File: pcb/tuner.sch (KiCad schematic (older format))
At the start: 39 parts, among them P1 PDI, SW1 SPST, SW2 <, SW3 >, SW4 Mode, U1 TPS62240, U2 NKR131SB, U3 ATXMEGA8E5, Y1 8 MHz

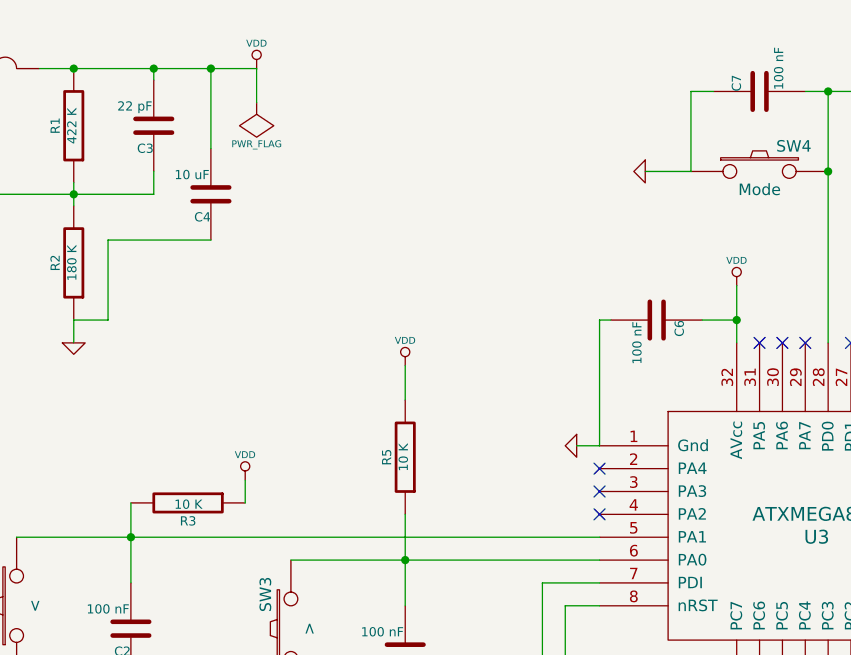
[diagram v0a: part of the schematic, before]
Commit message: - Added manufacturer, part number, and description fields to BOM - Changed MCU info to an equivalent that is available
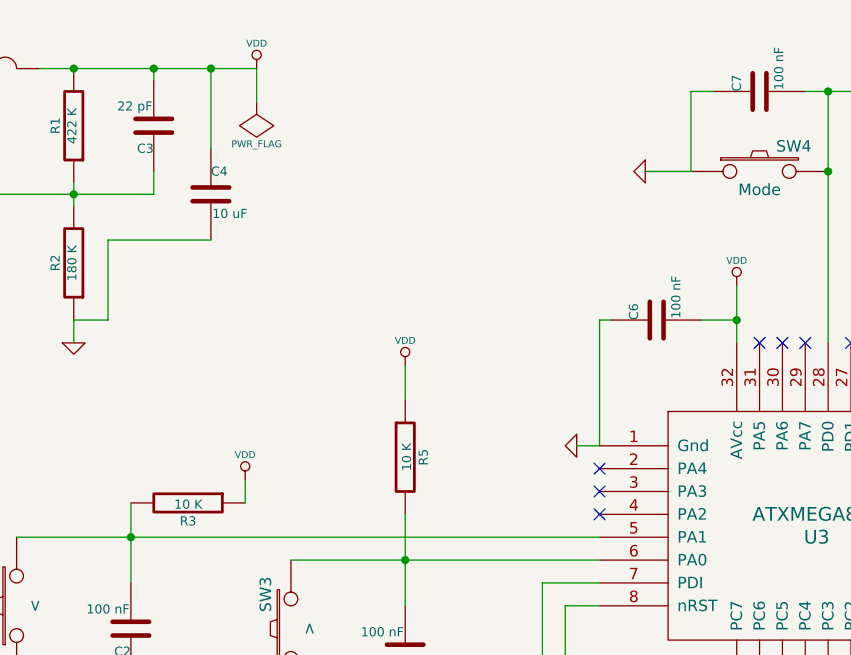
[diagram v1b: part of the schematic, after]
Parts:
- BT1: Desc (none) -> HOLDER BATT 2-AAA CELLS PC MOUNT; Manufacturer (none) -> MPD; P/N (none) -> BH2AAAPC
- C1, C4: Desc (none) -> CAP CER 10UF 6.3V 10% X5R 0805; Manufacturer (none) -> Yageo; P/N (none) -> CC0805KKX5R5BB106
- C10: Desc (none) -> CAP CER 27PF 50V 5% NP0 0805; Manufacturer (none) -> Kemet; P/N (none) -> C0805C270J5GACTU
- C2, C5, C6, C7, C8: Desc (none) -> CAP CER 0.1UF 50V 10% X7R 0805; Manufacturer (none) -> Kemet; P/N (none) -> C0805C104K5RACTU; URL http://www.digikey.ca/product-detail/en/CC0805KKX5R5BB106/3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 -> http://www.digikey.ca/product-detail/en/C0805C104K5RACTU/39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
- C3: Desc (none) -> CAP CER 22PF 50V 5% NP0 0805; Manufacturer (none) -> Kemet; P/N (none) -> C0805C220J5GACTU
- C9: Desc (none) -> CAP CER 25PF 50V 5% NP0 0805; Manufacturer (none) -> Samsung Electro-Mechanics America Inc; P/N (none) -> CL21C250JBANNNC
- D1, D2: Desc (none) -> LED 660NM SUPER RED CLR 0805 T/R; Manufacturer (none) -> Lumex Opto/Components Inc; P/N (none) -> SML-LX0805SRC-TR
- L1: Desc (none) -> INDUCTOR 2.2UH 20% 1008; Manufacturer (none) -> Murata Electronics North America; P/N (none) -> LQM2HPN2R2MJ0L
- R1: Desc (none) -> RES 422K OHM 1/8W 1% 0805 SMD; Manufacturer (none) -> Yageo; P/N (none) -> RC0805FR-07422KL
- R10, R11, R13, R14, R6, R7, R8, R9: Desc (none) -> RES 27 OHM 1/8W 1% 0805 SMD; Manufacturer (none) -> Panasonic Electronic Components; P/N (none) -> ERJ-6ENF27R0V
- R12, R3, R4, R5: Desc (none) -> RES 10.0K OHM 1/8W 1% 0805 SMD; Manufacturer (none) -> Yageo; P/N (none) -> RC0805FR-0710KL
- R15, R16: Desc (none) -> RES 18.0 OHM 1/8W 1% 0805 SMD; Manufacturer (none) -> Yageo; P/N (none) -> RC0805FR-0718RL
- R2: Desc (none) -> RES 180K OHM 1/8W 1% 0805 SMD; Manufacturer (none) -> Yageo; P/N (none) -> RC0805FR-07180KL
- SW1: Desc (none) -> SWITCH DIP SLIDE 1POS T/H 1MM 6V; Manufacturer (none) -> Copal Electronics Inc; P/N (none) -> CVS-01C
- SW2, SW3, SW4: Desc (none) -> SWITCH TACTILE SPST-NO 0.05A 12V; Manufacturer (none) -> Apem Inc.; P/N (none) -> MJTP1243
- U1: Desc (none) -> IC REG BUCK SYNC ADJ TSOT23-5; Manufacturer (none) -> Texas Instruments; P/N (none) -> TPS62240DDCT
- U2: Desc (none) -> LED 7SEG DISP .30\" RED CC BLACK; Manufacturer (none) -> Stanley Electric Co; P/N (none) -> NKR131SB
- U3: Desc (none) -> IC MCU 8BIT 8KB FLASH 32TQFP; Manufacturer (none) -> Atmel; P/N (none) -> ATXMEGA8E5-AU; URL http://www.digikey.ca/product-detail/en/ATXMEGA8E5-AUR/ATXM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 -> http://www.digikey.ca/product-detail/en/ATXMEGA8E5-AU/ATXME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
- Y1: Desc (none) -> CRYSTAL 8MHZ 18PF SMD; Manufacturer (none) -> TXC CORPORATION; P/N (none) -> 9C-8.000MEEJ-T
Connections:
- net GND: now also C4.2, C6.1; no longer C4.1, C6.2
- net VDD: now also C4.1, C6.2, R5.1; no longer C4.2, C6.1, R5.2
- net at C5.2, SW3.2, U3.6 (PA0): now also R5.2; no longer R5.1

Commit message: - Converted hardware design files to KiCAD 4.x format - Created footprints for new parts in r3 hardware design - Revised schematic and footprint associations for r3 hardware design
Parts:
- removed P1: PDI, symbol PDI
- removed R16: 18 Ohms, ~, symbol R
- removed SW1: SPST, ~, symbol SPST
- removed Y1: 8 MHz, ~, symbol CRYSTAL
- added P1: PDI, tuner:PDI_2x5, symbol SWDI
- added R16: 2.2 Ohms, Resistors_SMD:R_0603_HandSoldering, symbol R-RESCUE-tuner
- added SW1: Switch_SPDT_x2, tuner:SPDT, symbol Switch_SPDT_x2
- added Y1: 8 MHz, tuner:XTAL-SMD-4, symbol XTAL-4
- BT1: footprint (none) -> tuner:BATTERY
- C1, C4: footprint ~ -> Capacitors_SMD:C_0805_HandSoldering; symbol C -> C-RESCUE-tuner
- C10: value 27 pF -> 6.9 pF; footprint ~ -> Capacitors_SMD:C_0402; symbol C -> C-RESCUE-tuner
- C2, C3, C5, C6, C7, C8: footprint ~ -> Capacitors_SMD:C_0603_HandSoldering; symbol C -> C-RESCUE-tuner
- C9: value 25 pF -> 8.6 pF; footprint ~ -> Capacitors_SMD:C_0402; symbol C -> C-RESCUE-tuner
- D1, D2: footprint ~ -> LEDs:LED-5MM; symbol LED -> LED-RESCUE-tuner
- L1: footprint ~ -> tuner:SM1008
- R1, R10, R11, R12, R13, R14, R2, R3, R4, R5, R6, R7, R8, R9: footprint ~ -> Resistors_SMD:R_0603_HandSoldering; symbol R -> R-RESCUE-tuner
- R15: value 18 Ohms -> 2.2 Ohms; footprint ~ -> Resistors_SMD:R_0603_HandSoldering; symbol R -> R-RESCUE-tuner; Desc RES 18.0 OHM 1/8W 1% 0805 SMD -> RES SMD 2.2 OHM 1% 1/10W 0603; P/N RC0805FR-0718RL -> RC0603FR-072R2L; URL http://www.digikey.ca/product-detail/en/RC0805FR-0718RL/311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 -> https://www.digikey.ca/product-detail/en/yageo/RC0603FR-072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
- SW2, SW3, SW4: footprint ~ -> tuner:SWITCH_YAY
- U1: footprint ~ -> TO_SOT_Packages_SMD:SOT-23-5
- U2: footprint (none) -> tuner:LED_DISPLAY
- U3: footprint (none) -> Housings_QFP:TQFP-32_7x7mm_Pitch0.8mm
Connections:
- net labels added: DOWN_SWITCH, LED1, LED2, MODE_SWITCH, PDI, UP_SWITCH, XTAL1, XTAL2, nRST
- wire segments 144 -> 135
- no-connect marks 11 -> 12
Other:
- note added: "Parasitic capacitance:\nXTAL1 = 5.4 pF\nXTAL2 = 7.1 pF\n\nLoad capacitance = 10 pF\nStray capacitance = 3 pF\n\nCL = C^2 / 2C + Cstray\n\nC = 14 pF\nC9 = 14 pF - 5.4 pF = 8.6 pF\nC10 = 14 pF - 7.1 pF = 6.9 pF"
